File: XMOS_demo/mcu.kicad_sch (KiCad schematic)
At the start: 30 parts, among them J1 XSYS2 DEBUG CONNECTOR, U1 U316-1024-QF60B

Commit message: crystal, usb
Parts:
- added C20, C21: 18p, Capacitor_SMD:C_0603_1608Metric, symbol Device:C_Small
- added J2: USB_C_Receptacle_USB2.0_16P, Connector_USB:USB_C_Receptacle_GCT_USB4085, symbol Connector:USB_C_Receptacle_USB2.0_16P
- added R8: 1M, Resistor_SMD:R_0603_1608Metric, symbol Device:R_Small
- added R9: 680R, Resistor_SMD:R_0603_1608Metric, symbol Device:R_Small
- added U2: NUP2202, Package_TO_SOT_SMD:SOT-363_SC-70-6, symbol Power_Protection:NUP2202
- added Y1: Crystal_24M, Crystal:Crystal_SMD_2520-4Pin_2.5x2.0mm, symbol _Oscillator:Crystal_24M
- U1: footprint _QFN:QFN-60_7x7mm_P0.4mm_EP_ThermalVias_PowerBars -> _Package_QFN:QFN-60_7x7mm_P0.4mm_EP_ThermalVias_PowerBars
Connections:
- net GND: now also C20.2, C21.2, J2.A1 (GND), J2.A12 (GND), J2.B1 (GND), J2.B12 (GND), J2.S1 (SHIELD), U2.2, Y1.2 (G), Y1.4 (G)
- net at U1.15 (XOUT): now also R8.1, R9.1
- net at U1.16 (XIN): now also C21.1, R8.2, Y1.1
- net at U1.28 (USB_DM): now also J2.A7 (D-), J2.B7 (D-), U2.6
- net at U1.29 (USB_DP): now also J2.A6 (D+), J2.B6 (D+), U2.1
- new net: C20.1, R9.2, Y1.3
- new net VBUS: J2.A4 (VBUS), J2.A9 (VBUS), J2.B4 (VBUS), J2.B9 (VBUS), U2.5
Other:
- moved on the sheet: C1, C10, C11, C12, C13, C14, C15, C16, C17, C18, C19, C2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

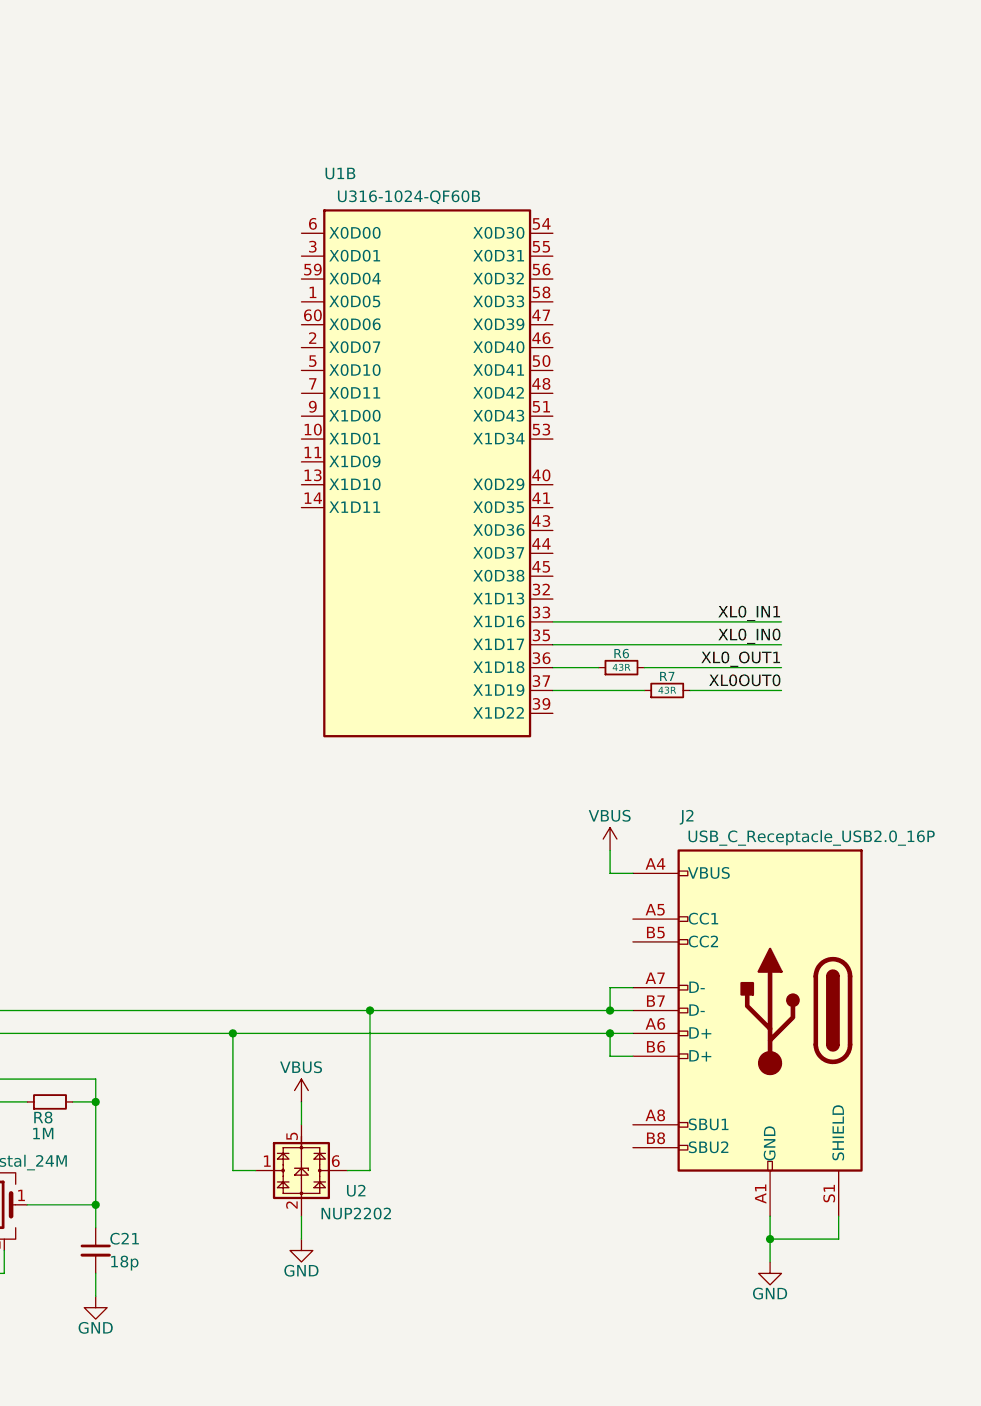
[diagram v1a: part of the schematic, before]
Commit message: leds, usb cc lines
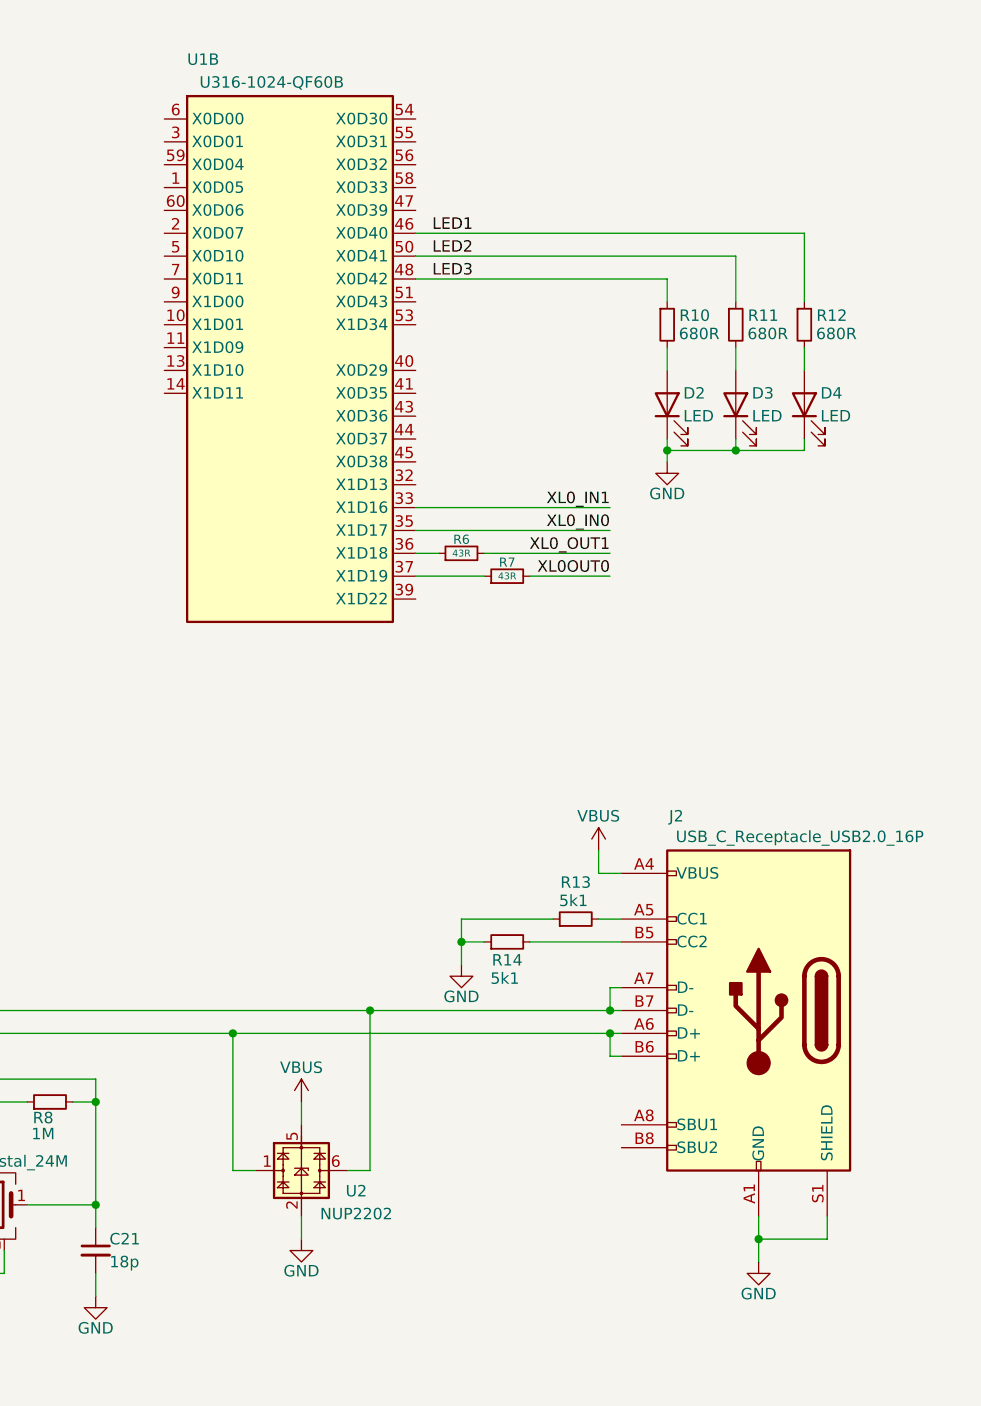
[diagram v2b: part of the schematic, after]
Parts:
- added D2, D3, D4: LED, LED_SMD:LED_0603_1608Metric, symbol Device:LED
- added R10, R11, R12: 680R, Resistor_SMD:R_0603_1608Metric, symbol Device:R_Small
- added R13, R14: 5k1, Resistor_SMD:R_0603_1608Metric, symbol Device:R_Small
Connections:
- net GND: now also D2.1 (K), D3.1 (K), D4.1 (K), R13.1, R14.1
- net at J2.A5 (CC1): now also R13.2
- net at J2.B5 (CC2): now also R14.2
- net LED1: now reaches U1.46 (X0D40)
- net LED1: now also R12.1
- net LED3: now reaches U1.48 (X0D42)
- net LED3: now also R10.1
- net LED2: now reaches U1.50 (X0D41)
- net LED2: now also R11.1
- new net: D2.2 (A), R10.2
- new net: D4.2 (A), R12.2
- new net: D3.2 (A), R11.2
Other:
- moved on the sheet: J2, R6, R7, U1B

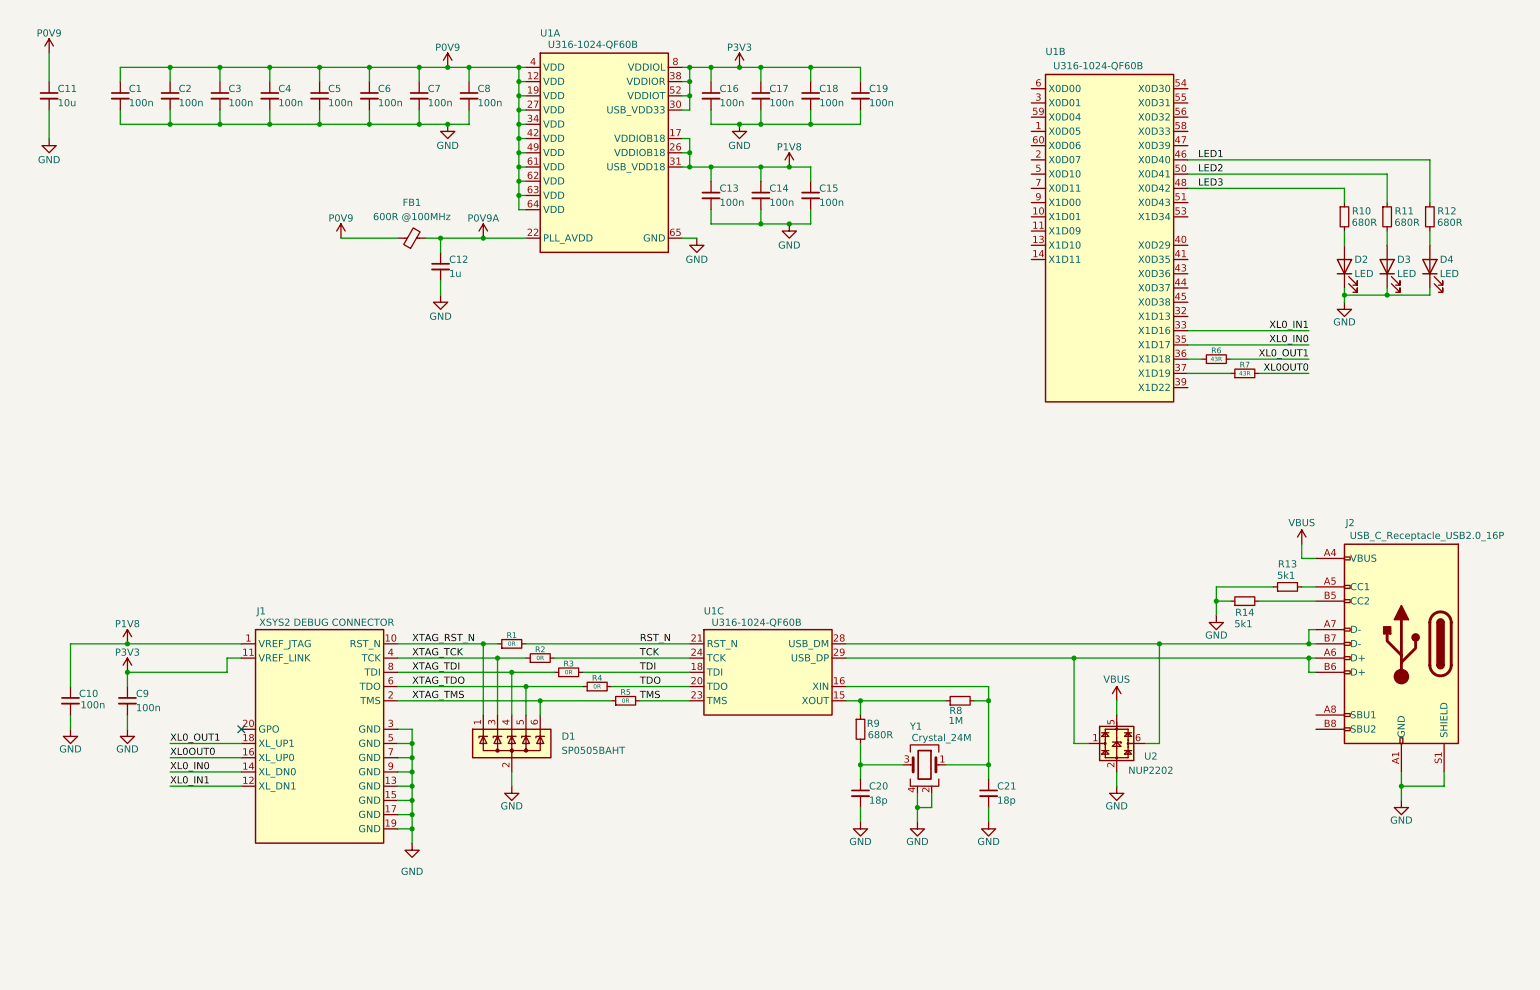
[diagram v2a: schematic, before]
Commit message: usb moved to seperate sch, power supply sch started
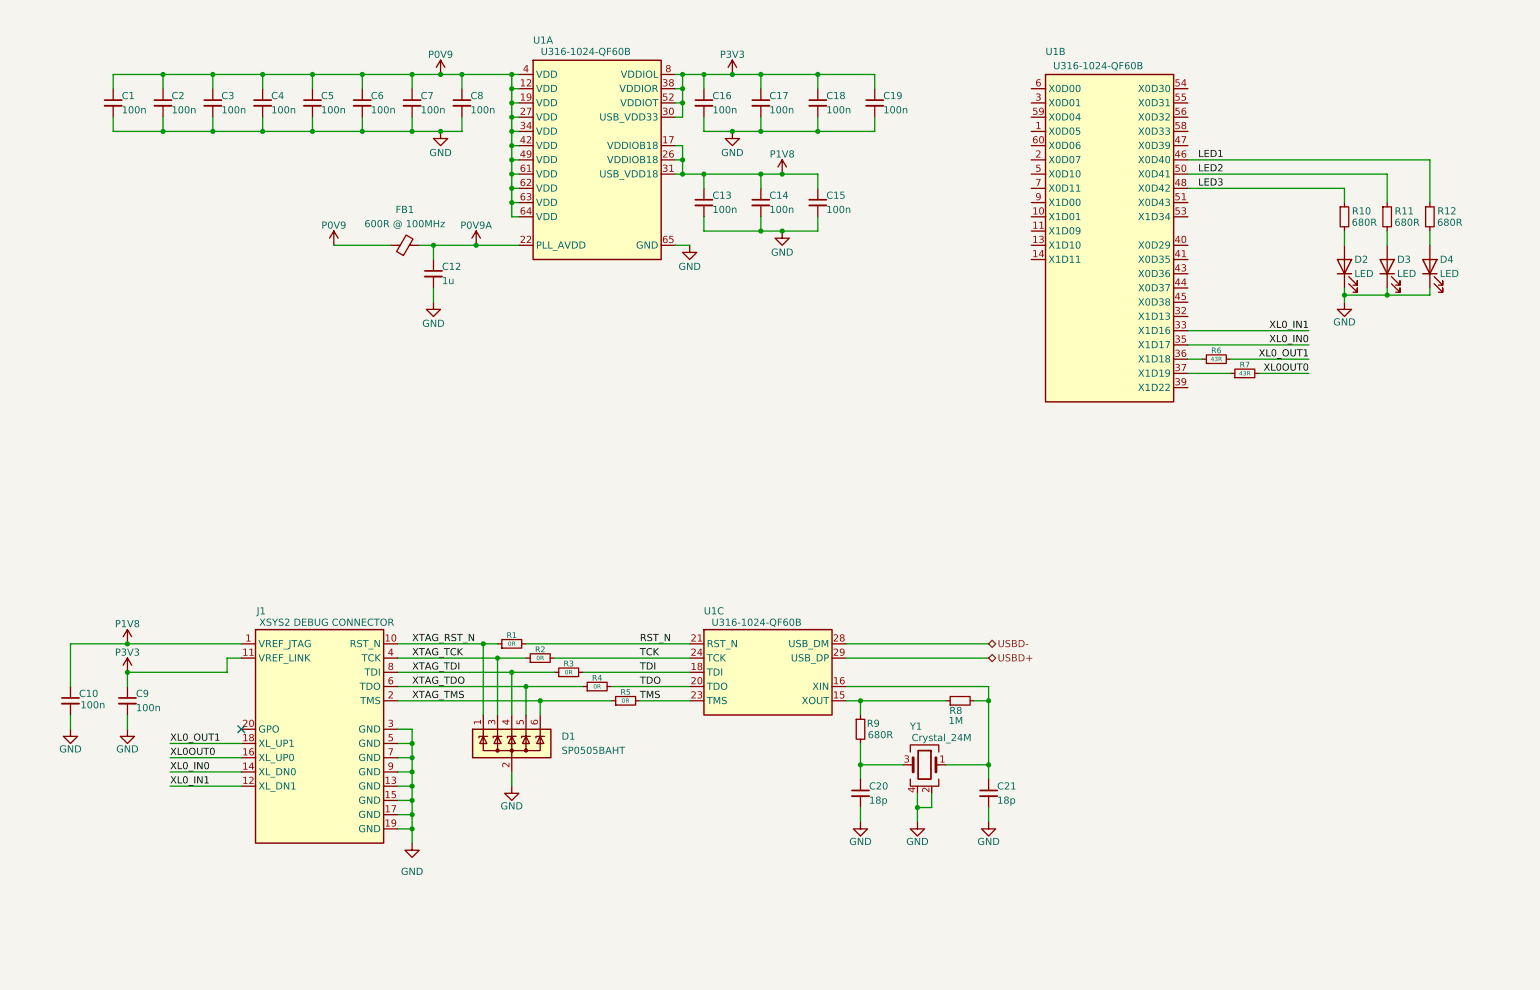
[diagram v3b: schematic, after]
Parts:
- removed C11: 10u, Capacitor_SMD:C_1206_3216Metric, symbol Device:C_Small
- removed J2: USB_C_Receptacle_USB2.0_16P, Connector_USB:USB_C_Receptacle_GCT_USB4085, symbol Connector:USB_C_Receptacle_USB2.0_16P
- removed R13, R14: 5k1, Resistor_SMD:R_0603_1608Metric, symbol Device:R_Small
- removed U2: NUP2202, Package_TO_SOT_SMD:SOT-363_SC-70-6, symbol Power_Protection:NUP2202
- C12: Max Voltage 10V -> 16V
- FB1: value 600R @100MHz -> 600R @ 100MHz; MPN BLM15HD601SN1D -> MI0603J601R-10
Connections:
- net USBD+: now reaches U1.29 (USB_DP)
- net USBD-: now reaches U1.28 (USB_DM)
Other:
- moved on the sheet: C1, C12, C13, C14, C15, C16, C17, C18, C19, C2, C3, C4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

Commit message: sch work
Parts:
- U1: footprint _Package_QFN:QFN-60_7x7mm_P0.4mm_EP_ThermalVias_PowerBars -> _QFN:QFN-60_7x7mm_P0.4mm_EP_ThermalVias_PowerBars; MPN (none) -> XU316-1024-QF60B-C24
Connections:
- net XL0OUT0 renamed XL0_OUT0
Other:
- company: (none) -> AGH University
- title: (none) -> USB Sound Card MCU
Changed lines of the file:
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@@
 	(generator_version "9.0")
 	(paper "A4")
+	(title_block
+		(title "USB Sound Card MCU")
+		(date "2026-03-29")
+		(rev "0.1")
+		(company "AGH University")
+	)
 	(junction
 		(at 97.79 127)
@@
 	(wire
 		(pts
+			(xy 231.14 76.2) (xy 246.38 76.2)
+		)
+		(stroke
+			(width 0)
+			(type default)
+		)
+	)
+	(wire
+		(pts
 			(xy 223.52 45.72) (xy 251.46 45.72)
 		)
@@
 	(wire
 		(pts
+			(xy 236.22 78.74) (xy 246.38 78.74)
+		)
+		(stroke
+			(width 0)
+			(type default)
+		)
+	)
+	(wire
+		(pts
 			(xy 102.87 35.56) (xy 104.14 35.56)
 		)
@@
 	(wire
 		(pts
+			(xy 223.52 73.66) (xy 246.38 73.66)
+		)
+		(stroke
+			(width 0)
+			(type default)
+		)
+	)
+	(wire
+		(pts
 			(xy 142.24 25.4) (xy 137.16 25.4)
 		)
@@
 	(wire
 		(pts
+			(xy 223.52 71.12) (xy 246.38 71.12)
+		)
+		(stroke
+			(width 0)
+			(type default)
+		)
+	)
+	(wire
+		(pts
 			(xy 88.9 63.5) (xy 88.9 66.04)
 		)
@@
 	(wire
 		(pts
-			(xy 231.14 76.2) (xy 245.11 76.2)
-		)
-		(stroke
-			(width 0)
-			(type default)
-		)
-	)
-	(wire
-		(pts
 			(xy 97.79 127) (xy 100.33 127)
 		)
@@
 	(wire
 		(pts
-			(xy 223.52 71.12) (xy 245.11 71.12)
-		)
-		(stroke
-			(width 0)
-			(type default)
-		)
-	)
-	(wire
-		(pts
 			(xy 251.46 53.34) (xy 251.46 55.88)
 		)
@@
 	(wire
 		(pts
-			(xy 236.22 78.74) (xy 245.11 78.74)
-		)
-		(stroke
-			(width 0)
-			(type default)
-		)
-	)
-	(wire
-		(pts
 			(xy 223.52 43.18) (xy 259.08 43.18)
 		)
@@
 	(wire
 		(pts
-			(xy 223.52 73.66) (xy 245.11 73.66)
-		)
-		(stroke
-			(width 0)
-			(type default)
-		)
-	)
-	(wire
-		(pts
 			(xy 102.87 40.64) (xy 102.87 43.18)
 		)
@@
 			(font
 				(size 1.27 1.27)
+				(color 0 194 0 1)
 			)
 			(justify left bottom)
 		)
 	)
-	(label "XL0OUT0"
+	(label "XL0_OUT0"
 		(at 41.91 147.32 0)
 		(effects
 			(font
 				(size 1.27 1.27)
+				(color 0 194 0 1)
 			)
 			(justify left bottom)
@@
 	)
 	(label "XL0_OUT1"
-		(at 245.11 76.2 180)
+		(at 246.38 76.2 180)
 		(effects
 			(font
 				(size 1.27 1.27)
+				(color 0 194 0 1)
 			)
 			(justify right bottom)
@@
 		)
 	)
-	(label "XL0OUT0"
-		(at 245.11 78.74 180)
+	(label "XL0_OUT0"
+		(at 246.38 78.74 180)
 		(effects
 			(font
 				(size 1.27 1.27)
+				(color 0 194 0 1)
 			)
 			(justify right bottom)
@@
 			(font
 				(size 1.27 1.27)
+				(color 0 194 0 1)
 			)
 			(justify left bottom)
@@
 			(font
 				(size 1.27 1.27)
+				(color 0 194 0 1)
 			)
 			(justify left bottom)
@@
 	)
 	(label "XL0_IN1"
-		(at 245.11 71.12 180)
+		(at 246.38 71.12 180)
 		(effects
 			(font
 				(size 1.27 1.27)
+				(color 0 194 0 1)
 			)
 			(justify right bottom)
@@
 	)
 	(label "XL0_IN0"
-		(at 245.11 73.66 180)
+		(at 246.38 73.66 180)
 		(effects
 			(font
 				(size 1.27 1.27)
+				(color 0 194 0 1)
 			)
 			(justify right bottom)
@@
 			)
 		)
-		(property "Footprint" "_Package_QFN:QFN-60_7x7mm_P0.4mm_EP_ThermalVias_PowerBars"
+		(property "Footprint" "_QFN:QFN-60_7x7mm_P0.4mm_EP_ThermalVias_PowerBars"
 			(at 195.58 27.94 0)
 			(effects
@@
 			)
 		)
+		(property "MPN" "XU316-1024-QF60B-C24"
+			(at 211.074 91.44 0)
+			(effects
+				(font
+					(size 1.27 1.27)
+				)
+				(hide yes)
+			)
+		)
 		(pin "42"
 		)
@@
 			)
 		)
-		(property "Footprint" "_Package_QFN:QFN-60_7x7mm_P0.4mm_EP_ThermalVias_PowerBars"
+		(property "Footprint" "_QFN:QFN-60_7x7mm_P0.4mm_EP_ThermalVias_PowerBars"
 			(at 134.62 127 0)
 			(effects
@@
 			)
 		)
+		(property "MPN" "XU316-1024-QF60B-C24"
+			(at 150.114 190.5 0)
+			(effects
+				(font
+					(size 1.27 1.27)
+				)
+				(hide yes)
+			)
+		)
 		(pin "42"
 		)
@@
 			)
 		)
-		(property "Footprint" "_Package_QFN:QFN-60_7x7mm_P0.4mm_EP_ThermalVias_PowerBars"
+		(property "Footprint" "_QFN:QFN-60_7x7mm_P0.4mm_EP_ThermalVias_PowerBars"
 			(at 104.14 25.4 0)
 			(effects
@@
 			(effects
 				(font
+					(size 1.27 1.27)
+				)
+				(hide yes)
+			)
+		)
+		(property "MPN" "XU316-1024-QF60B-C24"
+			(at 119.634 88.9 0)
+			(effects
+				(font

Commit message: Lots of sch work
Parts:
- C1, C10, C13, C14, C15, C16, C17, C18, C19, C2, C3, C4, C5, C6, C7, C8, C9: Max Voltage 10V -> 16V
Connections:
- net P0V9: now also U1.57 (VDD)
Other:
- moved on the sheet: C12, FB1

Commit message: sch work, pcb import and initial board outline
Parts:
- added C51: 100n, Capacitor_SMD:C_0603_1608Metric, symbol Device:C_Small
- added R35, R36: 0R, Resistor_SMD:R_0603_1608Metric, symbol Device:R_Small
- added R37: 5k1, Resistor_SMD:R_0603_1608Metric, symbol Device:R_Small
- added R41, R42: 4k7, Resistor_SMD:R_0603_1608Metric, symbol Device:R_Small
- added U6: W25Q32JVSS, Package_SO:SOIC-8_5.3x5.3mm_P1.27mm, symbol Memory_Flash:W25Q32JVSS
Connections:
- net GND: now also C51.1, U6.4 (GND)
- net P1V8: now also R36.1
- net P3V3: now also R35.1, R41.1, R42.1; no longer C16.1, U1.8 (VDDIOL)
- net QSPI_D1: now reaches U1.1 (X0D05)
- net QSPI_D1: now also U6.2 (DO/IO_{1})
- net QSPI_D3: now reaches U1.2 (X0D07)
- net QSPI_D3: now also U6.7 (~{HOLD}/~{RESET}/IO_{3})
- net QSPI_~{CS}: now reaches U1.3 (X0D01)
- net QSPI_~{CS}: now also R37.1, U6.1 (~{CS})
- net SCL: now reaches U1.41 (X0D35)
- net SCL: now also R41.2
- net SDA: now reaches U1.43 (X0D36)
- net SDA: now also R42.2
- net QSPI_CLK: now reaches U1.5 (X0D10)
- net QSPI_CLK: now also U6.6 (CLK)
- net QSPI_D0: now reaches U1.59 (X0D04)
- net QSPI_D0: now also U6.5 (DI/IO_{0})
- net QSPI_D2: now reaches U1.60 (X0D06)
- net QSPI_D2: now also U6.3 (~{WP}/IO_{2})
- new net P_IO_L: C16.1, C51.2, R35.2, R36.2, R37.2, U1.8 (VDDIOL), U6.8 (VCC)
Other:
- note added: "LOCKED INTO 3V3 FOR IO_L - PLL PIN, CODEC VOLTAGE, NEEDS FLASH FOR 3V3"
- note added: "TAKE CARE WITH IO_L SUPPLY CONFIGURATION DEPENDING ON AVIABLE QSPI FLASH"
- moved on the sheet: C1, C10, C12, C13, C14, C15, C16, C17, C18, C19, C2, C20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

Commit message: sch mostly finished, needs tp, pcb component layout started
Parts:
- renumbered C51 to C1, C8 to C10, C17 to C11, C18 to C12, C19 to C13, C13 to C14, C14 to C15, C15 to C16, C12 to C17, C10 to C18, C9 to C19, C16 to C2, C1 to C3, C2 to C4, C3 to C5, C4 to C6, C5 to C7, C6 to C8, C7 to C9, D2 to D1, D3 to D2, D4 to D3, D1 to D4, R10 to R1, R7 to R10, R1 to R11, R2 to R12, R3 to R13, R4 to R14, R5 to R15, R8 to R16, R9 to R17, R11 to R2, R12 to R3, R35 to R4, R37 to R5, R36 to R6, R41 to R7, R42 to R8, R6 to R9, U6 to U2
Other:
- moved on the sheet: D1, D2, D3, R1, R2, R3
